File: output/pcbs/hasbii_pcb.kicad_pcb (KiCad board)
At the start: 2 copper layers, 160.9 x 104.5 mm, 58 parts

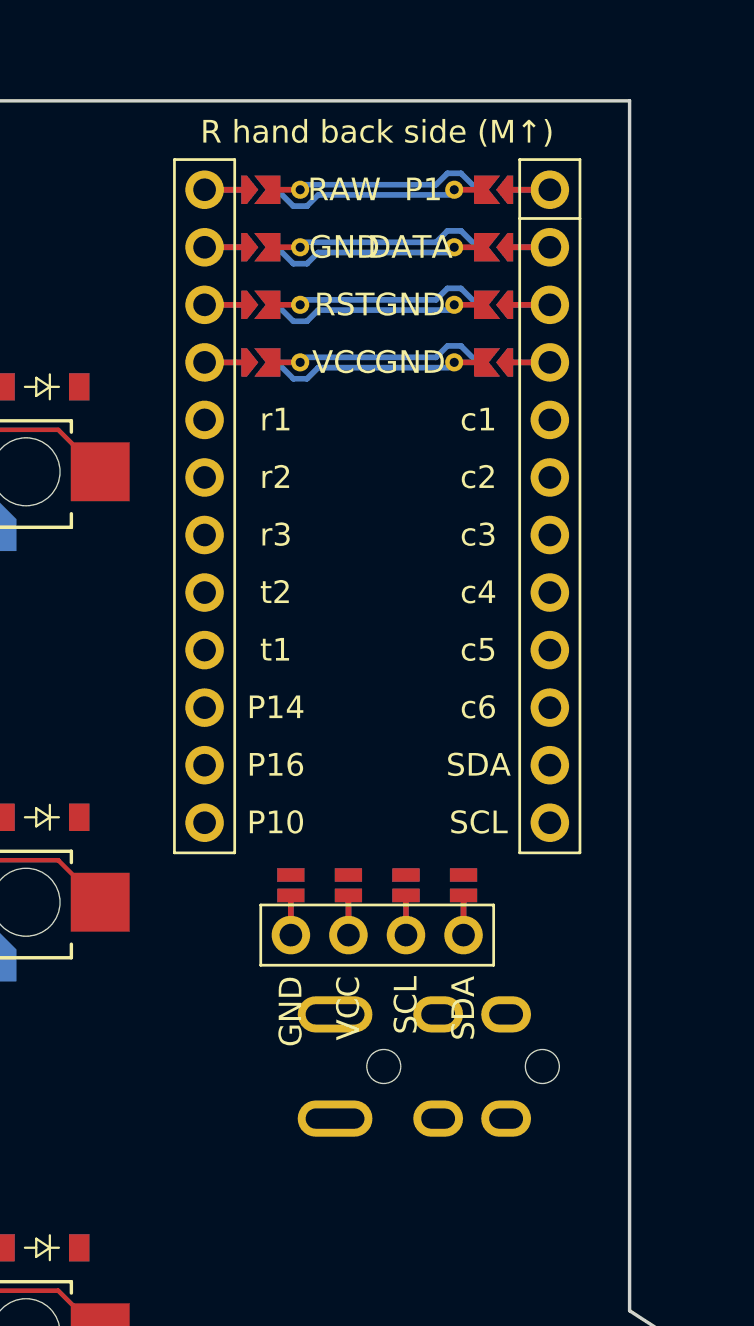
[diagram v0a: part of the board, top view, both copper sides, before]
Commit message: Add top frame outline and extrusion function for case design
- Implemented `_top_frame_extrude_3_outline_fn` to create the outline of the top frame using CSG.Path2D and CAG operations.
- Introduced `top_frame_case_fn` to generate the top frame part, including translation and rotation adjustments.
- Defined a `main` function to return the result of the top frame case function.
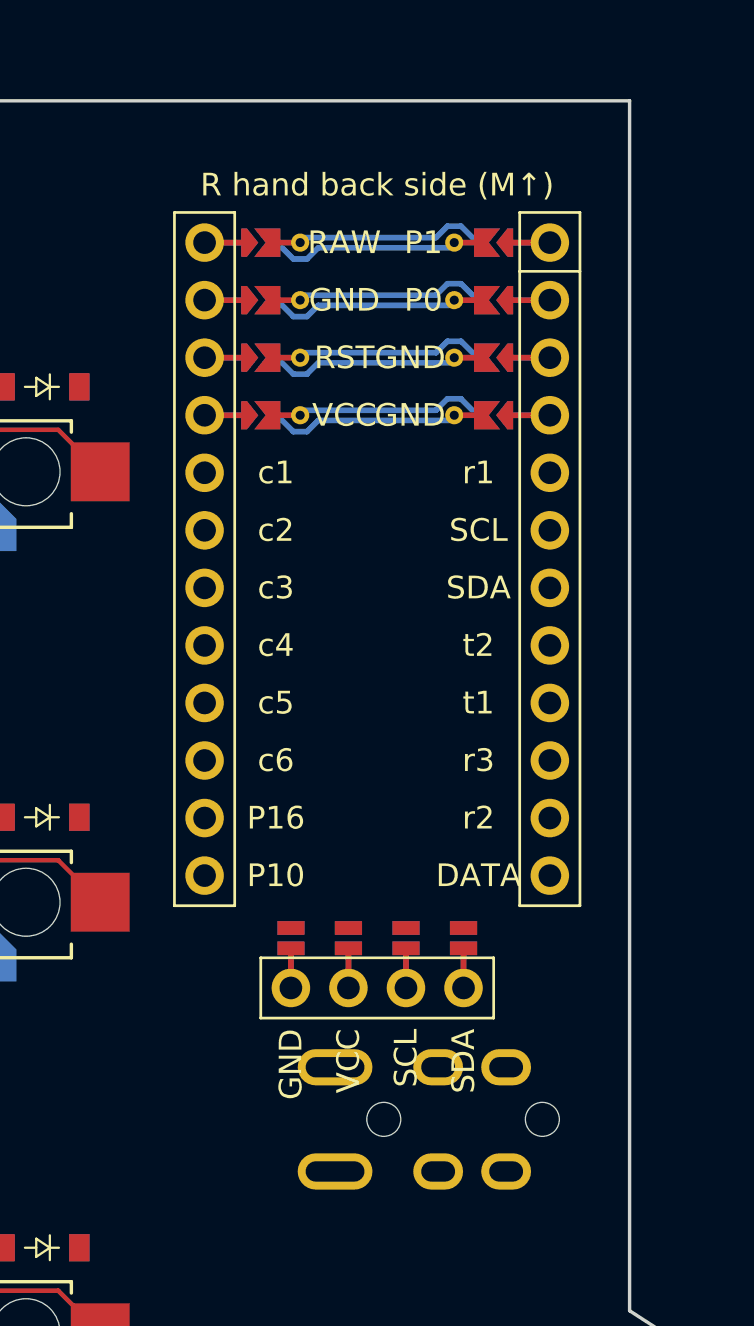
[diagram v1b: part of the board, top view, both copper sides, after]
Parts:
- moved DISP1 2.33 mm to (265.5, 121.8)
- moved MCU1 2.33 mm to (265.5, 118.3)
- moved TRRS1 2.33 mm to (274.4, 144.3)
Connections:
- MCU1 pad 10: c6 -> r3
- MCU1 pad 102: DATA -> P0
- MCU1 pad 11: SDA -> r2
- MCU1 pad 12: SCL -> DATA
- MCU1 pad 15: P14 -> c6
- MCU1 pad 16: t1 -> c5
- MCU1 pad 17: t2 -> c4
- MCU1 pad 18: r3 -> c3
- MCU1 pad 19: r2 -> c2
- MCU1 pad 20: r1 -> c1
- MCU1 pad 5: c1 -> r1
- MCU1 pad 6: c2 -> SCL
- MCU1 pad 7: c3 -> SDA
- MCU1 pad 8: c4 -> t2
- MCU1 pad 9: c5 -> t1
